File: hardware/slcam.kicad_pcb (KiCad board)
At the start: 4 copper layers, 42.2 x 27.4 mm, 37 parts, among them J1 532610671, J2 Conn_01x08, J3 Conn_01x04, J4 532610371, J5 532610371, U1 STM32F103C8T6, U2 W25Q128JVS, U3 TCAN330GD, U4 TPS2010AD, Y1 ECS-80-10-33-CHN-TR3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

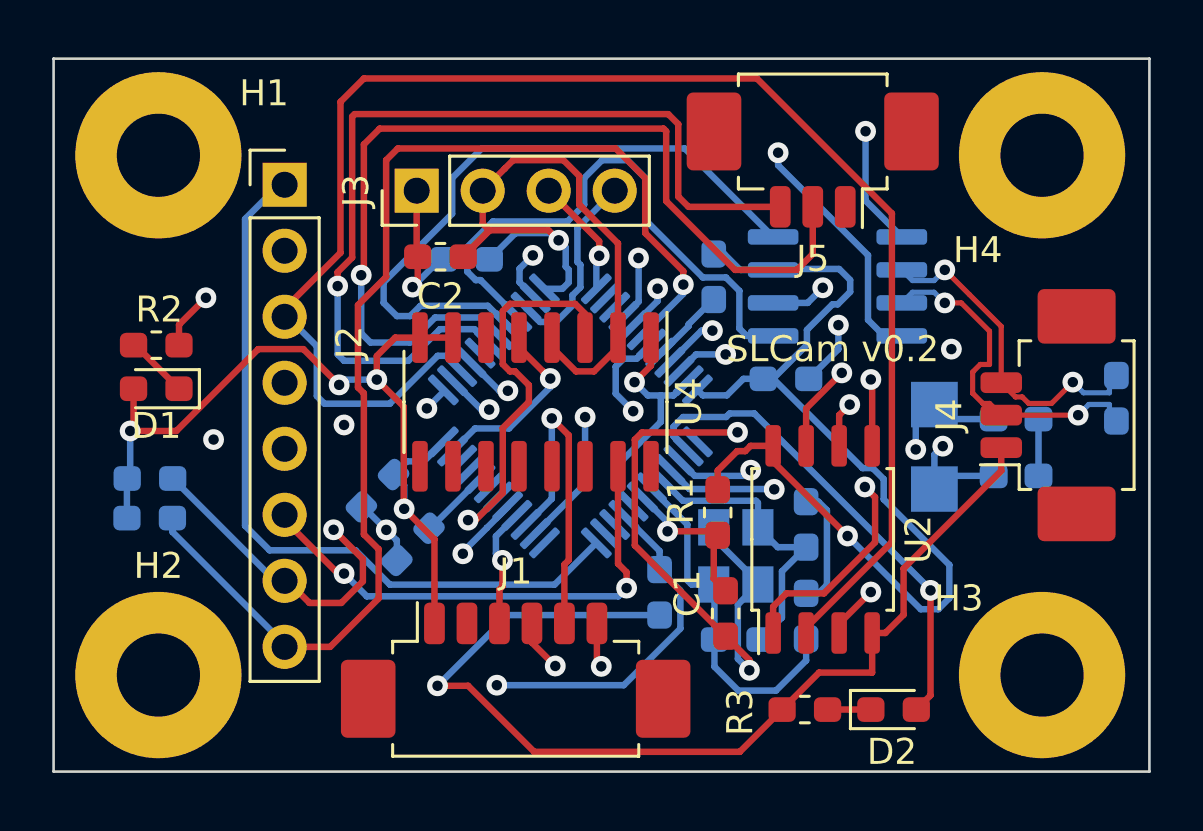
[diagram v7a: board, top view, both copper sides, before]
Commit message: hardware: Fixing J2 position
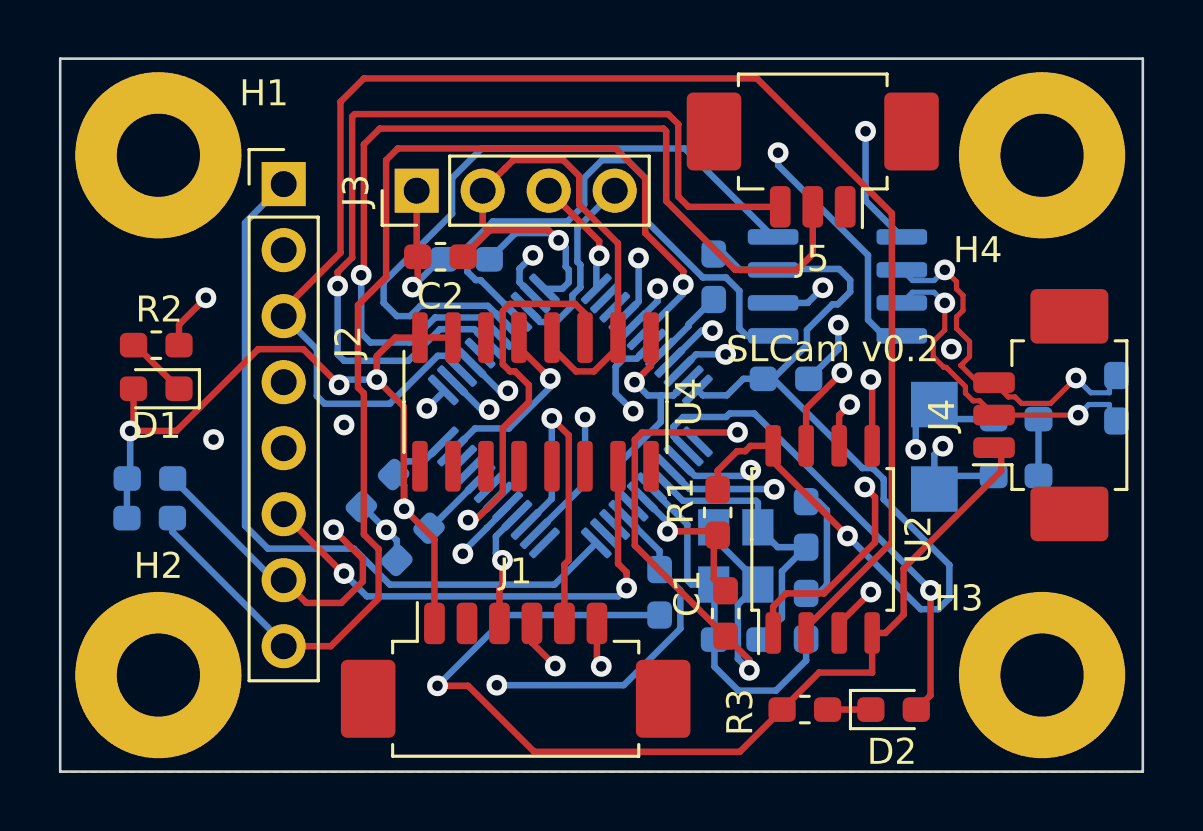
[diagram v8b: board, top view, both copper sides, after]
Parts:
- moved G*** 1.89 mm to (213.8, 74.3)
- moved J4 0.28 mm to (235.7, 62.5)
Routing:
- net /CAN_N: track 13.0 -> 14.2 mm
- net /CAN_P: track 13.6 -> 13.0 mm
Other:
- board size 42.2 x 27.4 mm -> 41.7 x 27.4 mm
- board text added: "0.2000 mm / 0.0000 mm"
- board text added: "0.3000 mm"
- board text added: "1.6600 mm"
- board text added: "41.6560 mm x 27.4320 mm"
- board text removed: "0,2000 mm / 0,0000 mm"
- board text removed: "0,3000 mm"
- board text removed: "1,6600 mm"
- board text removed: "42,2640 mm x 27,5320 mm"
